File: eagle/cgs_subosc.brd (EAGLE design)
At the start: 101.6 x 80.5 mm, 32 parts, among them IC1 TL072P, IC3 TL071P, IC4 4024N

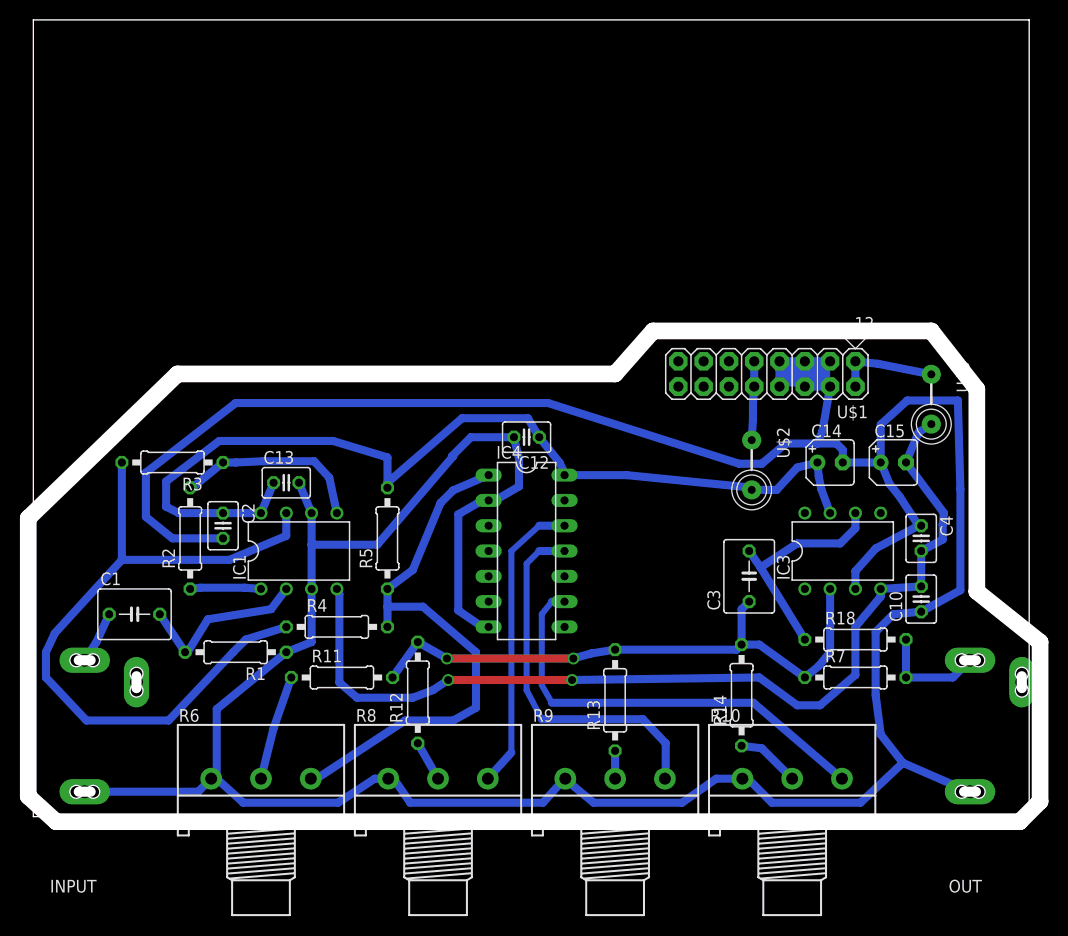
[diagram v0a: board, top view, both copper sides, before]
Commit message: verified then scrunched a little
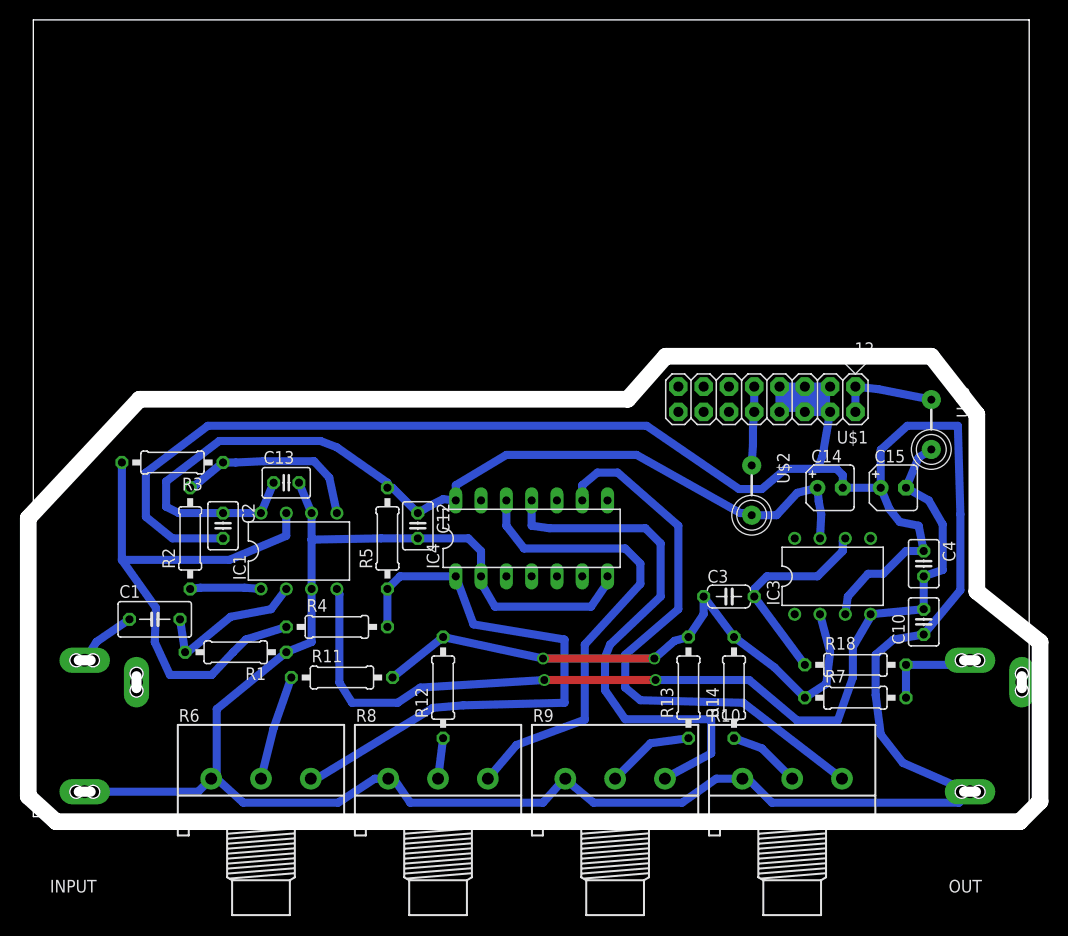
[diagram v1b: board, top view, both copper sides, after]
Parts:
- C1: device rcl:C050-050X075 -> rcl:C050-035X075
- C3: device rcl:C050-050X075 -> rcl:C050-024X044
- moved C12 14.1 mm to (38.6, 29.2), turned to 270 degrees
- moved R13 7.47 mm to (65.8, 13.0)
- moved C3 2.87 mm to (69.8, 22.1), turned to 0 degrees
- moved IC3 2.74 mm to (80.3, 24.1)
- moved R12 2.59 mm to (41.1, 13.0)
- moved C4 2.55 mm to (89.4, 25.4)
- moved U$1 2.54 mm to (76.2, 41.9)
- moved R18 2.54 mm to (82.5, 15.2)
- moved C14 2.54 mm to (80.0, 33.0)
- moved C15 2.54 mm to (86.4, 33.0)
- moved U$2 2.54 mm to (72.1, 32.8)
- moved U$3 2.54 mm to (90.2, 39.4)
- moved C10 2.30 mm to (89.4, 19.6)
- moved C1 2.09 mm to (12.2, 19.8)
- moved R7 2.03 mm to (82.5, 11.9)
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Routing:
- net N$5: track 73.4 -> 55.4 mm
- net N$18: track 30.1 -> 47.3 mm
- net N$19: track 37.4 -> 54.1 mm
- net N$20: track 44.0 -> 57.2 mm
- net GND: track 367.6 -> 358.9 mm
- net N$15: track 2.79 -> 8.87 mm
- net N$12: track 54.8 -> 59.4 mm
- net +12V: track 98.0 -> 95.9 mm
- net N$2: track 17.7 -> 15.9 mm
- net N$8: track 22.9 -> 21.1 mm
- net -12V: track 97.8 -> 99.5 mm
- net N$4: track 59.6 -> 61.1 mm
- net N$11: track 11.0 -> 9.92 mm
- net N$1: track 5.25 -> 6.20 mm
- net N$16: track 6.36 -> 7.28 mm
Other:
- outline, holes or cut-outs redrawn
